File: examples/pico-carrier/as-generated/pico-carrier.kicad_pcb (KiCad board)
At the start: 2 copper layers, 88 x 62 mm, 13 parts, among them J1 5V IN, J3 GP0-GP15, J4 GP16-GP28, PWR, U1 Pico

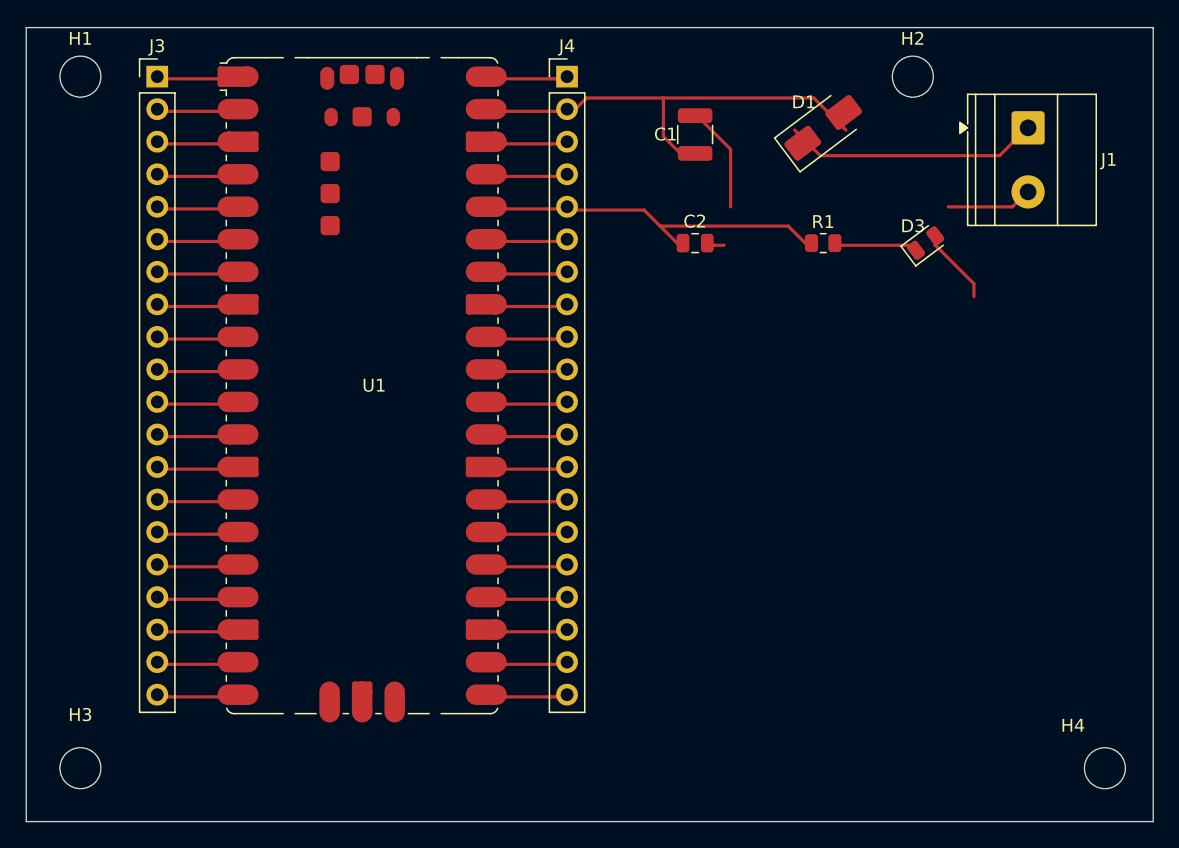
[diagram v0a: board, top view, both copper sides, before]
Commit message: Give the assembly machine something to aim at
Fiducials: three copper dots in bare mask windows, near three different
corners so a pick-and-place gets rotation as well as offset. It aligns
to the board, not to the drawing - without them it has only the routed
outline, cut to a tolerance ten times looser than the placement a 0.5 mm
pitch part is asking for. `fab.no_fiducials` reports a fine-pitch board
that has none, as context rather than as a fault: plenty of boards are
built one at a time with tweezers.

They share the corner search with the mounting holes, which is where
this found a real bug: `_courtyard_box` read lines and rectangles only,
and a mounting hole draws its courtyard as one circle - so every hole
measured as taking up no room at all, and the first three fiducials
landed on top of three screw holes. Circles and arcs count now.

Co-Authored-By: Claude Fable 5 <noreply@anthropic.com>
Claude-Session: https://claude.ai/code/session_01DUj7Ltu92tWg159mCSacwY
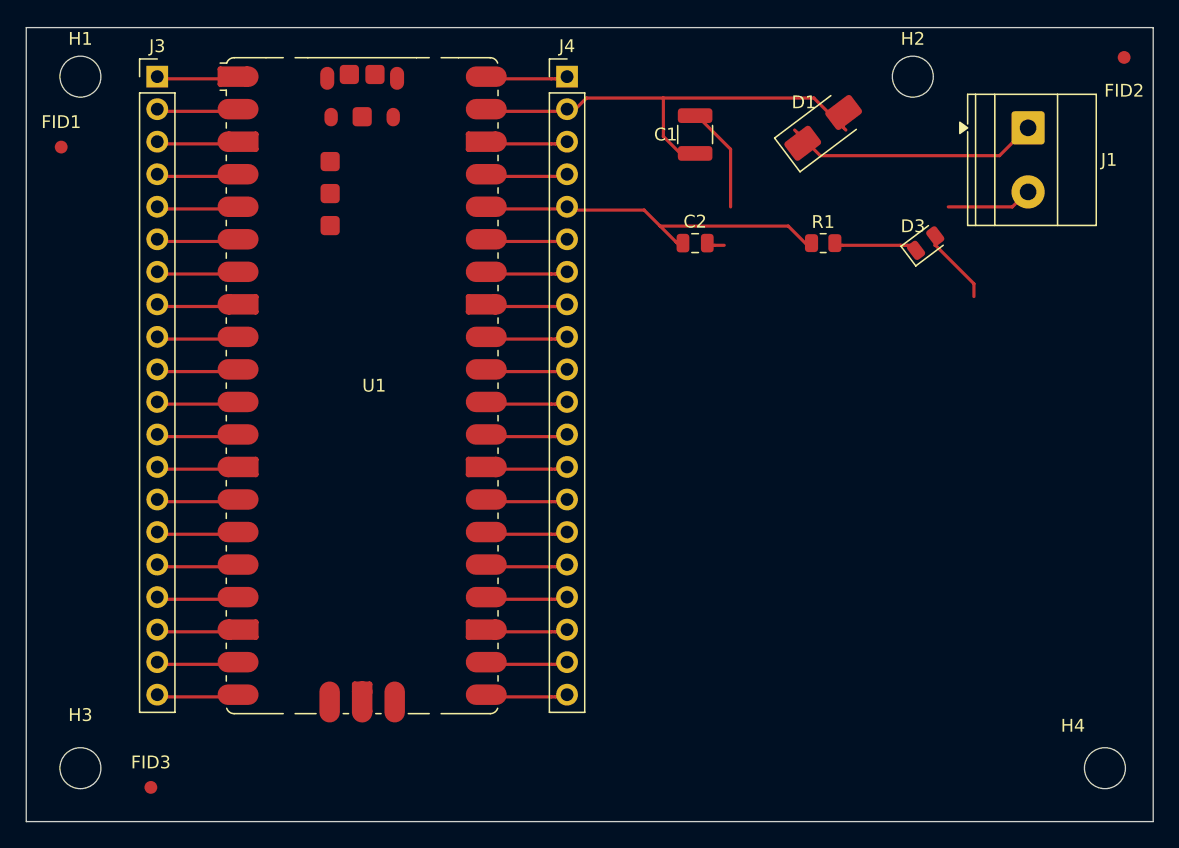
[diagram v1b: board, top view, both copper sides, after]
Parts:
- added FID1: Fiducial, Fiducial:Fiducial_1mm_Mask2mm, F.Cu at (102.7, 69.3)
- added FID2: Fiducial, Fiducial:Fiducial_1mm_Mask2mm, F.Cu at (185.7, 62.3)
- added FID3: Fiducial, Fiducial:Fiducial_1mm_Mask2mm, F.Cu at (109.7, 119.3)
- H1, H2, H3, H4: value M33 -> M3

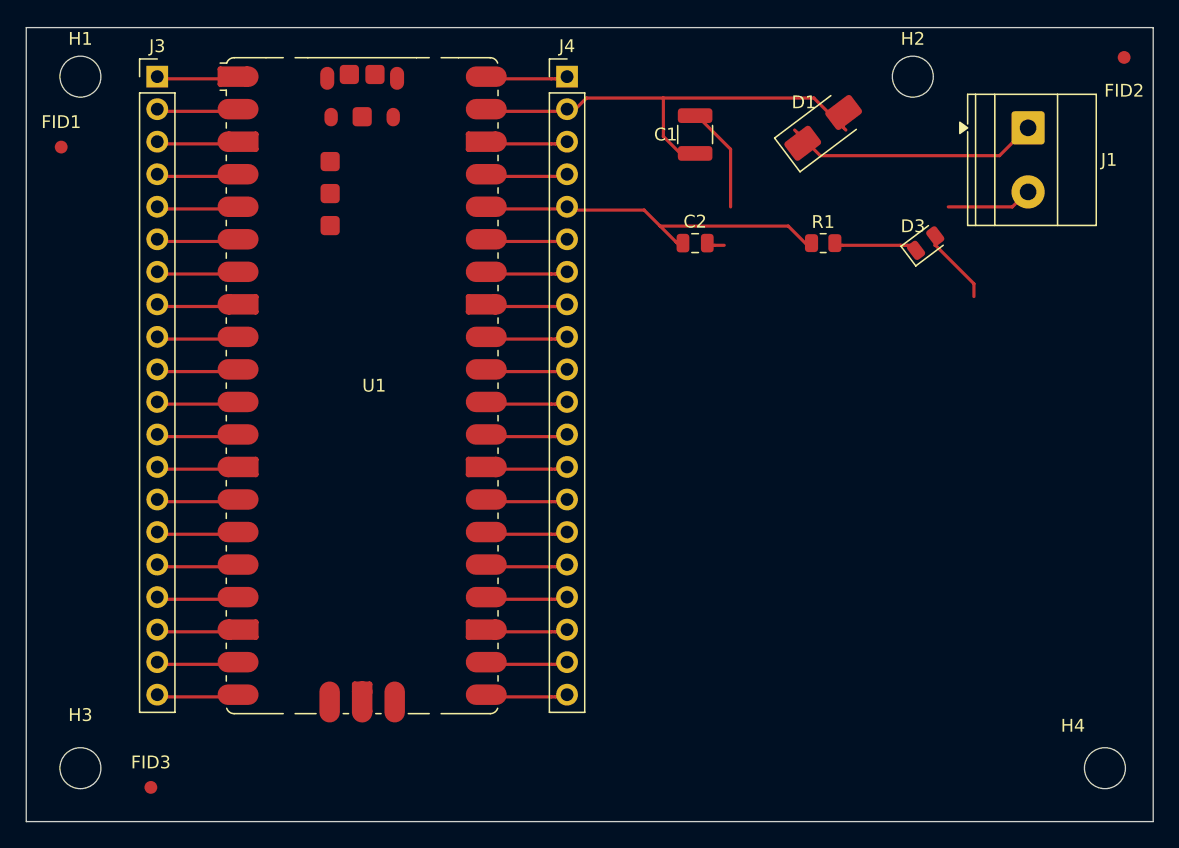
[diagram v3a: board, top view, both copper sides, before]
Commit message: Leave room for the screw, and print the ink where the board is
The screw holes were placed against the hole's own courtyard, which is the
drill plus a whisker - so on four of the five boards a hole sat inside a
connector's mating space, closest 0.42 mm. What goes through an M3 hole is a
pan head on a washer, seven millimetres of steel lying flat, and a connector
wants its shell, its wires and the fingers that fit them on top of that. The
spot search now keeps the fastener's own circle clear of every part body and
gives connectors CONNECTOR_ACCESS more, and three rules say so when a board
does not: mechanical.fastener_clearance, mechanical.connector_access and
mechanical.fastener_copper, all blocking for a generated design.

Silk was measured with a per-character advance of 0.78, and KiCad's stroke
font is proportional at 0.94 to 1.07. Everything downstream of that estimate
was placing ink where it did not fit: a legend across a capacitor's land, a
designator through the board's own name. `_text_extent` takes the top of the
measured range, adds the fab's clearance and is used by every silk placement.

Three placements also fell through to a position nobody chose. A designator
that found nothing kept its library offset, which for a part in a corner
points off the board; the board id took the first of eight fixed strips; a
legend took the least bad of six spots. All three are scored now, over
candidate sets wide enough to have an answer - and a pad-less footprint, which
is what a mounting hole is, is no longer skipped outright.

silk.off_board reports the case KiCad's own test cannot: ink that clears the
edge entirely is never printed, and DRC only measures ink that crosses it.

_unspiked redraws a corner tighter than a right angle as the elbow between its
neighbours - one diagonal, one straight, no step back to a heading the line
has already left. It is never longer than what it replaces.

All four fast boards: 0 errors, 0 warnings.

Co-Authored-By: Claude Fable 5 <no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
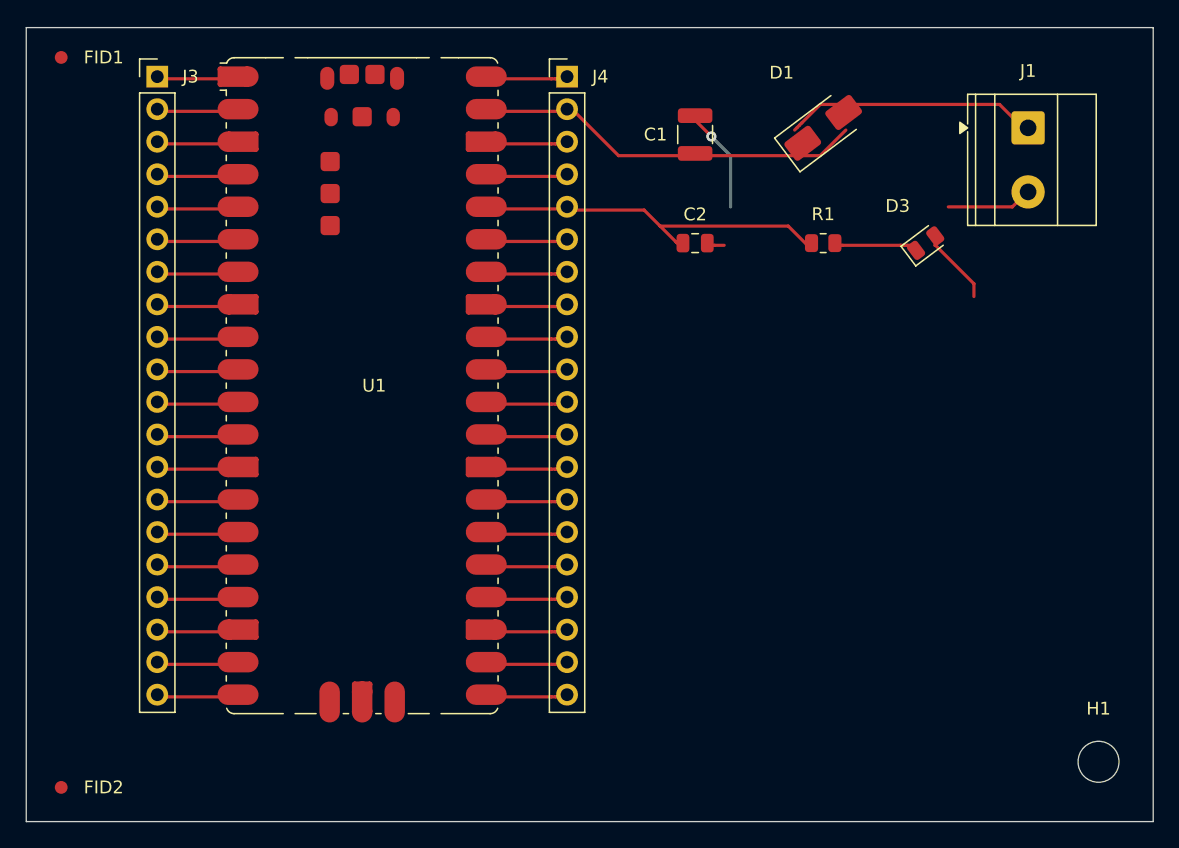
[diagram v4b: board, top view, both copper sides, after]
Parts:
- removed FID3: Fiducial, Fiducial:Fiducial_1mm_Mask2mm
- removed H2, H3, H4: M3, MountingHole:MountingHole_3.2mm_M3
- moved FID2 100.7 mm to (102.7, 119.3)
- moved H1 95.8 mm to (183.7, 117.3)
- moved FID1 7.00 mm to (102.7, 62.3)
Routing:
- net /VSYS: track 35.6 -> 30.6 mm
- net GND: track 60.7 -> 60.4 mm, vias 0 -> 1

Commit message: Walk the whole edge for a screw hole, and land a joint on its own pad
The fastener clearance was right and the search was not: it slid along two
edges from each corner and gave up, so boards that had had four screw holes
came back with one. It now walks a ring round the board at the inset the
screw needs, taking the nearest free point to each corner - and only from
that corner's own quarter, because a search that asked for the nearest free
point anywhere put three of the four along one edge, each of them the nearest
thing to a different corner. A quarter with no room gives no screw: three
that hold the board flat beat four that hold one side.

A pin header asks for nothing above its courtyard - the socket that fits it
lands inside the outline the header already draws - while a screw terminal's
wires leave horizontally from its face. Treating the two alike is what left a
carrier lined with headers with two holes on one edge. Both the generator and
the rule now tell them apart by footprint.

_landed folds a via that sits beside a plated hole of its own net onto the
hole. The plating already joins the faces, so the via bought nothing and cost
hole-to-hole: two drills a millimetre apart leave 0.15 mm of laminate at a
0.25 mm rule, which is what DRC reported on the opamp board.

The fillets move to the end of the pipeline. A taper is built against the end
of a run, and _landed moves ends, so a teardrop laid before it pointed at
where the run used to stop - a nought-degree corner in the angle rule.

buck-5v, motor-driver, pico-carrier, opamp-filter: 0 errors, 0 warnings.

Co-Authored-By: Claude Fable 5 <noreply@anthropic.com>
Claude-Session: https://claude.ai/code/session_01DUj7Ltu92tWg159mCSacwY
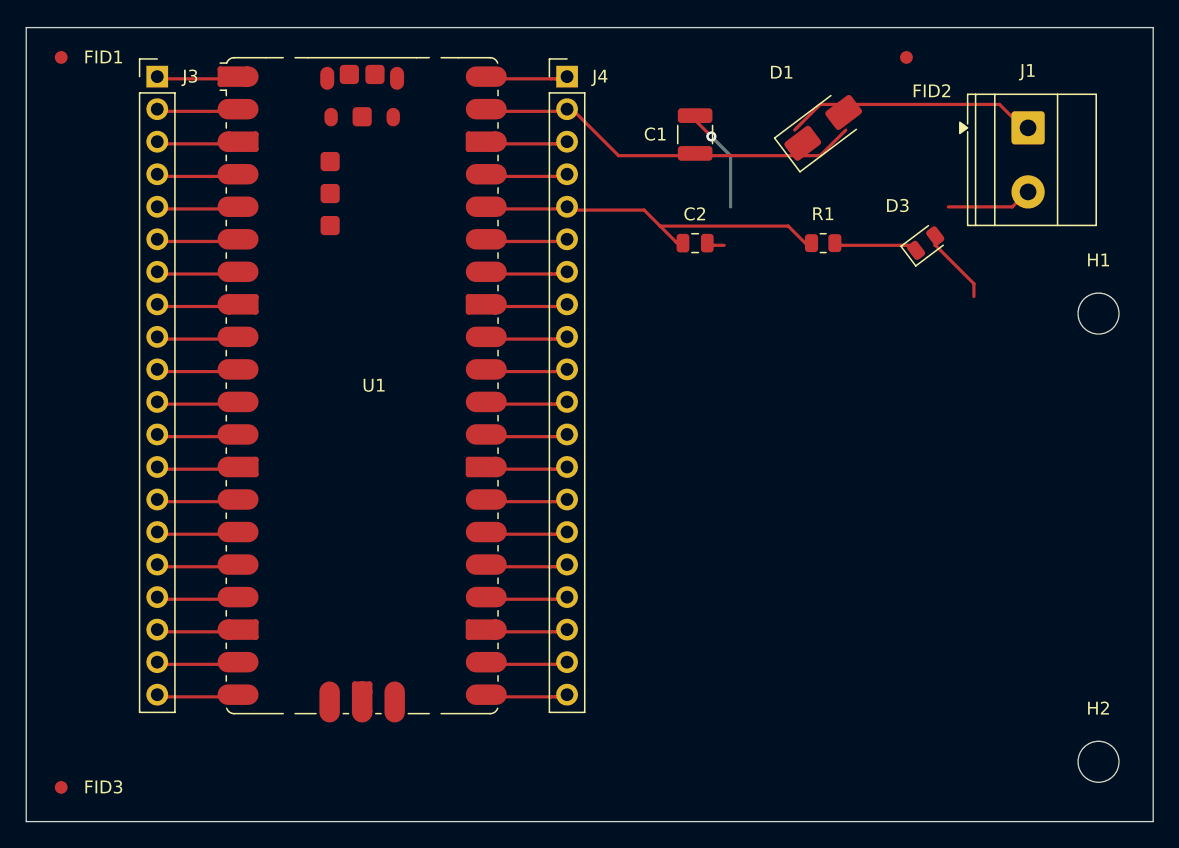
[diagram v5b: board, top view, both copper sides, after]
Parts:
- added FID3: Fiducial, Fiducial:Fiducial_1mm_Mask2mm, F.Cu at (102.7, 119.3)
- added H2: M3, MountingHole:MountingHole_3.2mm_M3, F.Cu at (183.7, 117.3)
- moved FID2 87.2 mm to (168.7, 62.3), turned to 37 degrees
- moved H1 35.0 mm to (183.7, 82.3)
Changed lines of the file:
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@@
 	(footprint "Fiducial:Fiducial_1mm_Mask2mm"
 		(layer "F.Cu")
-		(at 102.73 119.33)
+		(at 168.73 62.33 37)
 		(descr "Fiducial, circular marking, 1mm bare copper, 2mm soldermask opening (Level A)")
 		(tags "fiducial")
 		(property "Reference" "FID2"
-			(at 3.315 0 0)
+			(at 0 3.315 0)
 			(layer "F.SilkS")
 			(effects
@@
 		)
 		(property "Datasheet" "~"
-			(at 3.315 0 0)
+			(at 0 3.315 0)
 			(layer "F.Fab")
 			(hide yes)
@@
 		)
 		(property "Description" ""
-			(at 0 0 0)
+			(at 0 0 37)
 			(layer "F.Fab")
 			(hide yes)
@@
 		)
 		(pad "" smd circle
-			(at 0 0)
+			(at 0 0 37)
 			(size 1 1)
 			(layers "F.Cu" "F.Mask")
@@
 	(footprint "MountingHole:MountingHole_3.2mm_M3"
 		(layer "F.Cu")
-		(at 183.73 117.33)
+		(at 183.73 82.33)
 		(descr "Mounting Hole 3.2mm, M3, no annular, generated by kicad-footprint-generator mountinghole.py")
 		(tags "mountinghole M3")
@@
 		)
 	)
+	(footprint "MountingHole:MountingHole_3.2mm_M3"
+		(layer "F.Cu")
+		(at 183.73 117.33)
+		(descr "Mounting Hole 3.2mm, M3, no annular, generated by kicad-footprint-generator mountinghole.py")
+		(tags "mountinghole M3")
+		(property "Reference" "H2"
+			(at 0 -4.15 0)
+			(layer "F.SilkS")
+			(effects
+				(font
+					(size 1 1)
+					(thickness 0.15)
+				)
+			)
+		)
+		(property "Value" "M3"
+			(at 0 4.15 0)
+			(layer "F.Fab")
+			(effects
+				(font
+					(size 1 1)
+					(thickness 0.15)
+				)
+			)
+		)
+		(property "Datasheet" "~"
+			(at 0 -4.15 0)
+			(layer "F.Fab")
+			(hide yes)
+			(effects
+				(font
+					(size 1 1)
+					(thickness 0.15)
+				)
+			)
+		)
+		(property "Description" ""
+			(at 0 0 0)
+			(layer "F.Fab")
+			(hide yes)
+			(effects
+				(font
+					(size 1.27 1.27)
+					(thickness 0.15)
+				)
+			)
+		)
+		(attr exclude_from_pos_files exclude_from_bom)
+		(fp_circle
+			(center 0 0)
+			(end 3.2 0)
+			(stroke
+				(width 0.15)
+				(type solid)
+			)
+			(fill no)
+			(layer "Cmts.User")
+		)
+		(fp_circle
+			(center 0 0)
+			(end 3.45 0)
+			(stroke
+				(width 0.05)
+				(type solid)
+			)
+			(fill no)
+			(layer "F.CrtYd")
+		)
+		(fp_text user "${REFERENCE}"
+			(at 0 0 0)
+			(layer "F.Fab")
+			(effects
+				(font
+					(size 1 1)
+					(thickness 0.15)
+				)
+			)
+		)
+		(pad "" np_thru_hole circle
+			(at 0 0)
+			(size 3.2 3.2)
+			(drill 3.2)
+			(layers "*.Cu" "*.Mask")
+		)
+		(embedded_fonts no)
+	)
+	(footprint "Fiducial:Fiducial_1mm_Mask2mm"
+		(layer "F.Cu")
+		(at 102.73 119.33)
+		(descr "Fiducial, circular marking, 1mm bare copper, 2mm soldermask opening (Level A)")
+		(tags "fiducial")
+		(property "Reference" "FID3"
+			(at 3.315 0 0)
+			(layer "F.SilkS")
+			(effects
+				(font
+					(size 1 1)
+					(thickness 0.15)
+				)
+			)
+		)
+		(property "Value" "Fiducial"
+			(at 0 1.95 0)
+			(layer "F.Fab")
+			(effects
+				(font
+					(size 1 1)
+					(thickness 0.15)
+				)
+			)
+		)
+		(property "Datasheet" "~"
+			(at 3.315 0 0)
+			(layer "F.Fab")
+			(hide yes)
+			(effects
+				(font
+					(size 1 1)
+					(thickness 0.15)
+				)
+			)
+		)
+		(property "Description" ""
+			(at 0 0 0)
+			(layer "F.Fab")
+			(hide yes)
+			(effects
+				(font
+					(size 1.27 1.27)
+					(thickness 0.15)
+				)
+			)
+		)
+		(attr smd exclude_from_bom)
+		(fp_circle
+			(center 0 0)
+			(end 1.25 0)
+			(stroke
+				(width 0.05)
+				(type solid)
+			)
+			(fill no)
+			(layer "F.CrtYd")
+		)
+		(fp_circle
+			(center 0 0)
+			(end 1 0)
+			(stroke
+				(width 0.1)
+				(type solid)
+			)
+			(fill no)
+			(layer "F.Fab")
+		)
+		(fp_text user "${REFERENCE}"
+			(at 0 0 0)
+			(layer "F.Fab")
+			(effects
+				(font
+					(size 0.5 0.5)
+					(thickness 0.08)
+				)
+			)
+		)
+		(pad "" smd circle
+			(at 0 0)
+			(size 1 1)
+			(layers "F.Cu" "F.Mask")
+			(solder_mask_margin 0.5)
+			(clearance 0.6)
+		)
+		(embedded_fonts no)
+	)
 	(footprint "Diode_SMD:D_SMA"
